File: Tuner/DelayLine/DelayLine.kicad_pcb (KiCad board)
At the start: 2 copper layers, 100 x 100 mm, 88 parts, among them J1 Conn_Coaxial, J10 Conn_Coaxial, J11 Conn_Coaxial, J12 Conn_Coaxial, J13 Conn_01x01, J14 Conn_01x01, J15 Conn_01x01, J16 Conn_01x01, J17 Conn_02x10_Odd_Even, J18 Conn_Coaxial, J19 Conn_Coaxial, J2 Conn_01x01, J20 Conn_Coaxial, J21 Conn_Coaxial, J22 Conn_Coaxial, J23 Conn_Coaxial, J24 Conn_01x01, J25 Conn_01x01, J26 Conn_01x01, J27 Conn_01x01, J28 Conn_01x01, J29 Conn_Coaxial, J3 Conn_Coaxial, J31 Conn_Coaxial, J32 Conn_01x01, J33 Conn_01x01, J34 Conn_01x01, J35 Conn_01x01, J5 Conn_Coaxial, J6 Conn_Coaxial, J7 Conn_Coaxial, J8 Conn_01x02, J9 Conn_01x02

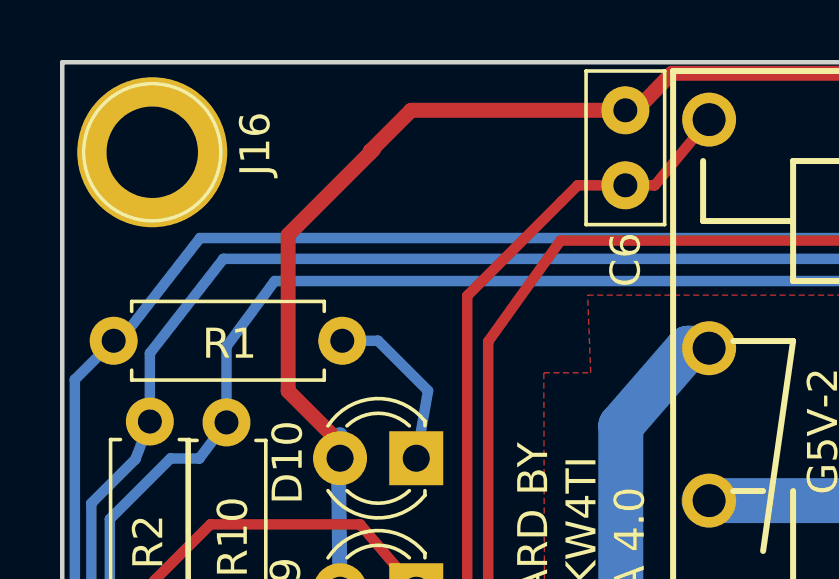
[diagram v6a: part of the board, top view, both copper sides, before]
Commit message: Added extra capacitors to ground to large relay boards
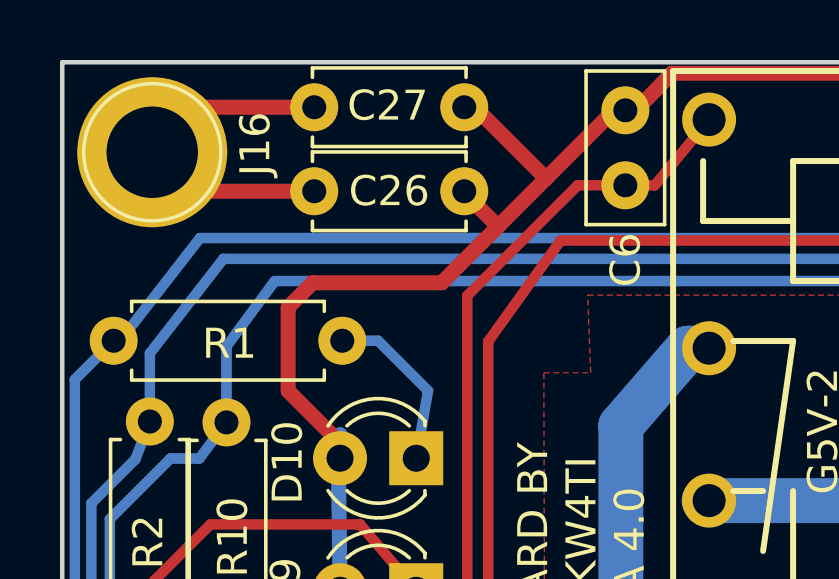
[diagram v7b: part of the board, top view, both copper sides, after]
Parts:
- added C26: 10 nF, Capacitors_THT:C_Disc_D5.0mm_W2.5mm_P5.00mm, F.Cu at (58.4, 54.3)
- added C27: 10 nF, Capacitors_THT:C_Disc_D5.0mm_W2.5mm_P5.00mm, F.Cu at (58.4, 51.5)
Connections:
- J16 pad 1: (no net) -> Net-(C26-Pad1)
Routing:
- net Net-(C26-Pad1): track 0.00 -> 12.0 mm
- net +5V: track 450.7 -> 454.4 mm
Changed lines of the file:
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@@
 (kicad_pcb (version 4) (host pcbnew 4.0.7)
   (general
-    (links 228)
+    (links 232)
     (no_connects 0)
     (area 44.941618 46.85238 155.4408 151.075)
     (thickness 1.6)
     (drawings 35)
-    (tracks 779)
+    (tracks 788)
     (zones 0)
-    (modules 88)
-    (nets 64)
+    (modules 90)
+    (nets 65)
   )
   (page A4)
@@
   (net 62 "Net-(C12-Pad1)")
   (net 63 "Net-(C13-Pad1)")
+  (net 64 "Net-(C26-Pad1)")
   (net_class Default "This is the default net class."
     (clearance 0.2)
@@
     (add_net "Net-(C12-Pad1)")
     (add_net "Net-(C13-Pad1)")
+    (add_net "Net-(C26-Pad1)")
     (add_net "Net-(D1-Pad1)")
     (add_net "Net-(D10-Pad1)")
@@
     (fp_circle (center 0 0) (end 2.6 0) (layer F.CrtYd) (width 0.05))
     (fp_circle (center 0 0) (end 0 -2.286) (layer F.SilkS) (width 0.12))
-    (pad 1 thru_hole circle (at 0 0) (size 5 5) (drill 3.048) (layers *.Cu *.Mask))
+    (pad 1 thru_hole circle (at 0 0) (size 5 5) (drill 3.048) (layers *.Cu *.Mask)
+      (net 64 "Net-(C26-Pad1)"))
   )
   (module Connectors:bnc-ci (layer F.Cu)
@@
     )
   )
+  (module Capacitors_THT:C_Disc_D5.0mm_W2.5mm_P5.00mm (layer F.Cu)
+    (at 58.4 54.3)
+    (descr "C, Disc series, Radial, pin pitch=5.00mm, , diameter*width=5*2.5mm^2, Capacitor, http://cdn-reichelt.de/documents/datenblatt/B300/DS_KERKO_TC.pdf")
+    (tags "C Disc series Radial pin pitch 5.00mm  diameter 5mm width 2.5mm Capacitor")
+    (fp_text reference C26 (at 2.5 0) (layer F.SilkS)
+      (effects (font (size 1 1) (thickness 0.15)))
+    )
+    (fp_text value "10 nF" (at 2.5 2.56) (layer F.Fab)
+      (effects (font (size 1 1) (thickness 0.15)))
+    )
+    (fp_line (start 0 -1.25) (end 0 1.25) (layer F.Fab) (width 0.1))
+    (fp_line (start 0 1.25) (end 5 1.25) (layer F.Fab) (width 0.1))
+    (fp_line (start 5 1.25) (end 5 -1.25) (layer F.Fab) (width 0.1))
+    (fp_line (start 5 -1.25) (end 0 -1.25) (layer F.Fab) (width 0.1))
+    (fp_line (start -0.06 -1.31) (end 5.06 -1.31) (layer F.SilkS) (width 0.12))
+    (fp_line (start -0.06 1.31) (end 5.06 1.31) (layer F.SilkS) (width 0.12))
+    (fp_line (start -0.06 -1.31) (end -0.06 -0.996) (layer F.SilkS) (width 0.12))
+    (fp_line (start -0.06 0.996) (end -0.06 1.31) (layer F.SilkS) (width 0.12))
+    (fp_line (start 5.06 -1.31) (end 5.06 -0.996) (layer F.SilkS) (width 0.12))
+    (fp_line (start 5.06 0.996) (end 5.06 1.31) (layer F.SilkS) (width 0.12))
+    (fp_line (start -1.05 -1.6) (end -1.05 1.6) (layer F.CrtYd) (width 0.05))
+    (fp_line (start -1.05 1.6) (end 6.05 1.6) (layer F.CrtYd) (width 0.05))
+    (fp_line (start 6.05 1.6) (end 6.05 -1.6) (layer F.CrtYd) (width 0.05))
+    (fp_line (start 6.05 -1.6) (end -1.05 -1.6) (layer F.CrtYd) (width 0.05))
+    (fp_text user %R (at 2.5 0) (layer F.Fab)
+      (effects (font (size 1 1) (thickness 0.15)))
+    )
+    (pad 1 thru_hole circle (at 0 0) (size 1.6 1.6) (drill 0.8) (layers *.Cu *.Mask)
+      (net 64 "Net-(C26-Pad1)"))
+    (pad 2 thru_hole circle (at 5 0) (size 1.6 1.6) (drill 0.8) (layers *.Cu *.Mask)
+      (net 12 +5V))
+    (model ${KISYS3DMOD}/Capacitors_THT.3dshapes/C_Disc_D5.0mm_W2.5mm_P5.00mm.wrl
+      (at (xyz 0 0 0))
+      (scale (xyz 1 1 1))
+      (rotate (xyz 0 0 0))
+    )
+  )
+  (module Capacitors_THT:C_Disc_D5.0mm_W2.5mm_P5.00mm (layer F.Cu)
+    (at 58.4 51.5)
+    (descr "C, Disc series, Radial, pin pitch=5.00mm, , diameter*width=5*2.5mm^2, Capacitor, http://cdn-reichelt.de/documents/datenblatt/B300/DS_KERKO_TC.pdf")
+    (tags "C Disc series Radial pin pitch 5.00mm  diameter 5mm width 2.5mm Capacitor")
+    (fp_text reference C27 (at 2.45 -0.05) (layer F.SilkS)
+      (effects (font (size 1 1) (thickness 0.15)))
+    )
+    (fp_text value "10 nF" (at 2.5 2.56) (layer F.Fab)
+      (effects (font (size 1 1) (thickness 0.15)))
+    )
+    (fp_line (start 0 -1.25) (end 0 1.25) (layer F.Fab) (width 0.1))
+    (fp_line (start 0 1.25) (end 5 1.25) (layer F.Fab) (width 0.1))
+    (fp_line (start 5 1.25) (end 5 -1.25) (layer F.Fab) (width 0.1))
+    (fp_line (start 5 -1.25) (end 0 -1.25) (layer F.Fab) (width 0.1))
+    (fp_line (start -0.06 -1.31) (end 5.06 -1.31) (layer F.SilkS) (width 0.12))
+    (fp_line (start -0.06 1.31) (end 5.06 1.31) (layer F.SilkS) (width 0.12))
+    (fp_line (start -0.06 -1.31) (end -0.06 -0.996) (layer F.SilkS) (width 0.12))
+    (fp_line (start -0.06 0.996) (end -0.06 1.31) (layer F.SilkS) (width 0.12))
+    (fp_line (start 5.06 -1.31) (end 5.06 -0.996) (layer F.SilkS) (width 0.12))
+    (fp_line (start 5.06 0.996) (end 5.06 1.31) (layer F.SilkS) (width 0.12))
+    (fp_line (start -1.05 -1.6) (end -1.05 1.6) (layer F.CrtYd) (width 0.05))
+    (fp_line (start -1.05 1.6) (end 6.05 1.6) (layer F.CrtYd) (width 0.05))
+    (fp_line (start 6.05 1.6) (end 6.05 -1.6) (layer F.CrtYd) (width 0.05))
+    (fp_line (start 6.05 -1.6) (end -1.05 -1.6) (layer F.CrtYd) (width 0.05))
+    (fp_text user %R (at 2.5 0) (layer F.Fab)
+      (effects (font (size 1 1) (thickness 0.15)))
+    )
+    (pad 1 thru_hole circle (at 0 0) (size 1.6 1.6) (drill 0.8) (layers *.Cu *.Mask)
+      (net 64 "Net-(C26-Pad1)"))
+    (pad 2 thru_hole circle (at 5 0) (size 1.6 1.6) (drill 0.8) (layers *.Cu *.Mask)
+      (net 12 +5V))
+    (model ${KISYS3DMOD}/Capacitors_THT.3dshapes/C_Disc_D5.0mm_W2.5mm_P5.00mm.wrl
+      (at (xyz 0 0 0))
+      (scale (xyz 1 1 1))
+      (rotate (xyz 0 0 0))
+    )
+  )
   (gr_text GND (at 144.6276 69.2912) (layer F.SilkS)
     (effects (font (size 1 1) (thickness 0.15)))
@@
   (segment (start 56.77408 91.83878) (end 62.34938 91.83878) (width 0.35) (layer B.Cu) (net 11))
   (segment (start 62.34938 91.83878) (end 63.6524 93.1418) (width 0.35) (layer B.Cu) (net 11) (status 20))
+  (segment (start 63.4 54.3) (end 63.4 54.35) (width 0.5) (layer F.Cu) (net 12))
+  (segment (start 63.4 54.35) (end 64.525 55.475) (width 0.5) (layer F.Cu) (net 12))
+  (segment (start 63.4 51.5) (end 63.75 51.5) (width 0.5) (layer F.Cu) (net 12))
+  (segment (start 63.75 51.5) (end 66.125 53.875) (width 0.5) (layer F.Cu) (net 12))
+  (segment (start 68.7705 51.602) (end 68.398 51.602) (width 0.5) (layer F.Cu) (net 12))
+  (segment (start 68.398 51.602) (end 66.125 53.875) (width 0.5) (layer F.Cu) (net 12))
+  (segment (start 66.125 53.875) (end 64.525 55.475) (width 0.5) (layer F.Cu) (net 12))
+  (segment (start 64.525 55.475) (end 62.65 57.35) (width 0.5) (layer F.Cu) (net 12))
+  (segment (start 58.35 57.35) (end 57.531 58.169) (width 0.5) (layer F.Cu) (net 12))
+  (segment (start 62.65 57.35) (end 58.35 57.35) (width 0.5) (layer F.Cu) (net 12))
   (segment (start 140.716 51.856) (end 137.9698 51.856) (width 0.5) (layer F.Cu) (net 12))
   (segment (start 137.9698 51.856) (end 137.9628 51.849) (width 0.5) (layer F.Cu) (net 12))
@@
   (segment (start 77.6302 50.3682) (end 79.1618 51.9125) (width 0.5) (layer F.Cu) (net 12) (status 20))
   (segment (start 70.3199 50.3682) (end 77.6302 50.3682) (width 0.5) (layer F.Cu) (net 12))
-  (segment (start 60.2615 53.0225) (end 60.2615 52.9717) (width 0.5) (layer F.Cu) (net 12))
-  (segment (start 61.6312 51.602) (end 68.7705 51.602) (width 0.5) (layer F.Cu) (net 12))
-  (segment (start 60.2615 52.9717) (end 61.6312 51.602) (width 0.5) (layer F.Cu) (net 12))
   (segment (start 127.6858 148.5119) (end 130.2174 148.5119) (width 0.5) (layer F.Cu) (net 12))
   (segment (start 130.2174 148.5119) (end 130.5025 148.2268) (width 0.5) (layer F.Cu) (net 12))
@@
   (segment (start 59.26 63.2) (end 59.26 62.689) (width 0.5) (layer F.Cu) (net 12))
   (segment (start 59.26 62.689) (end 57.531 60.96) (width 0.5) (layer F.Cu) (net 12))
-  (segment (start 57.531 55.753) (end 60.2615 53.0225) (width 0.5) (layer F.Cu) (net 12))
-  (segment (start 60.2615 53.0225) (end 60.3885 52.8955) (width 0.5) (layer F.Cu) (net 12))
-  (segment (start 57.531 60.96) (end 57.531 55.753) (width 0.5) (layer F.Cu) (net 12))
+  (segment (start 57.531 60.96) (end 57.531 58.169) (width 0.5) (layer F.Cu) (net 12))
   (segment (start 59.26 67.6) (end 59.26 68.24144) (width 0.5) (layer F.Cu) (net 12))
   (segment (start 124.0563 51.7728) (end 123.9317 51.7728) (width 0.5) (layer F.Cu) (net 12) (status 30))
@@
   (segment (start 146.812 53.188) (end 147 53) (width 1) (layer F.Cu) (net 63) (status 30))
   (segment (start 145.308 51.308) (end 147 53) (width 0.5) (layer F.Cu) (net 63) (status 30))
+  (segment (start 58.4 54.3) (end 54.3 54.3) (width 0.5) (layer F.Cu) (net 64))
+  (segment (start 54.3 54.3) (end 53 53) (width 0.5) (layer F.Cu) (net 64))
+  (segment (start 58.4 51.5) (end 54.5 51.5) (width 0.5) (layer F.Cu) (net 64))
+  (segment (start 54.5 51.5) (end 53 53) (width 0.5) (layer F.Cu) (net 64))
   (zone (net 1) (net_name RFGND) (layer F.Cu) (hatch edge 0.508)
     (connect_pads (clearance 1))
